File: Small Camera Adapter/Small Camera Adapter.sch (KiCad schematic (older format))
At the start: 6 parts, among them J1 68611514122, J2 10137062-00021LF

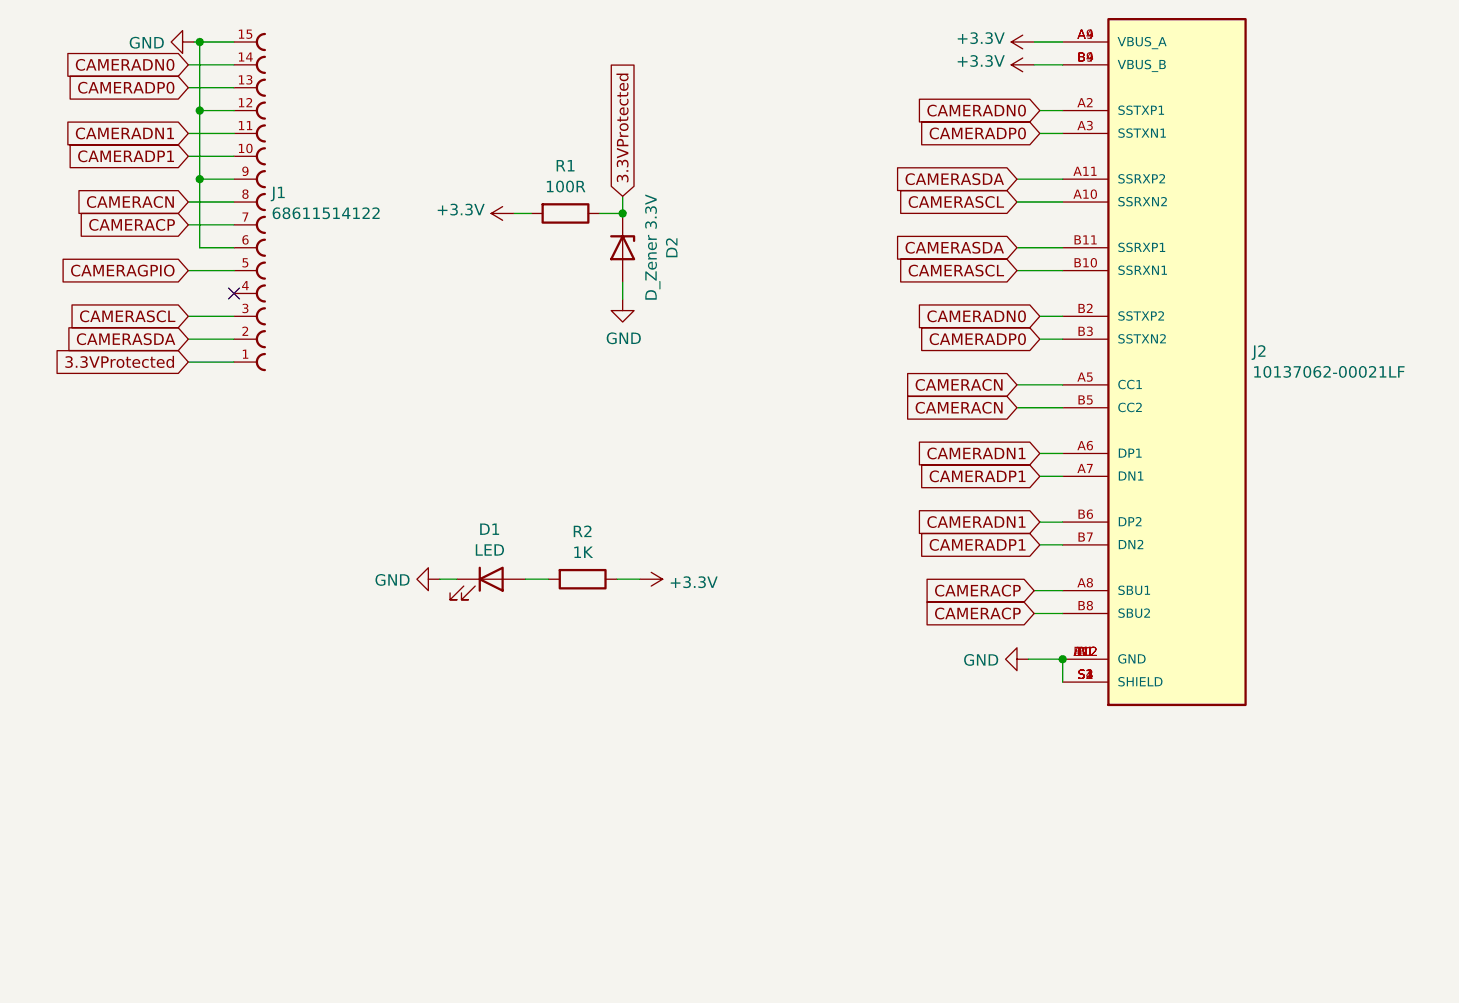
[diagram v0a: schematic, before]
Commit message: Update to camera adapter
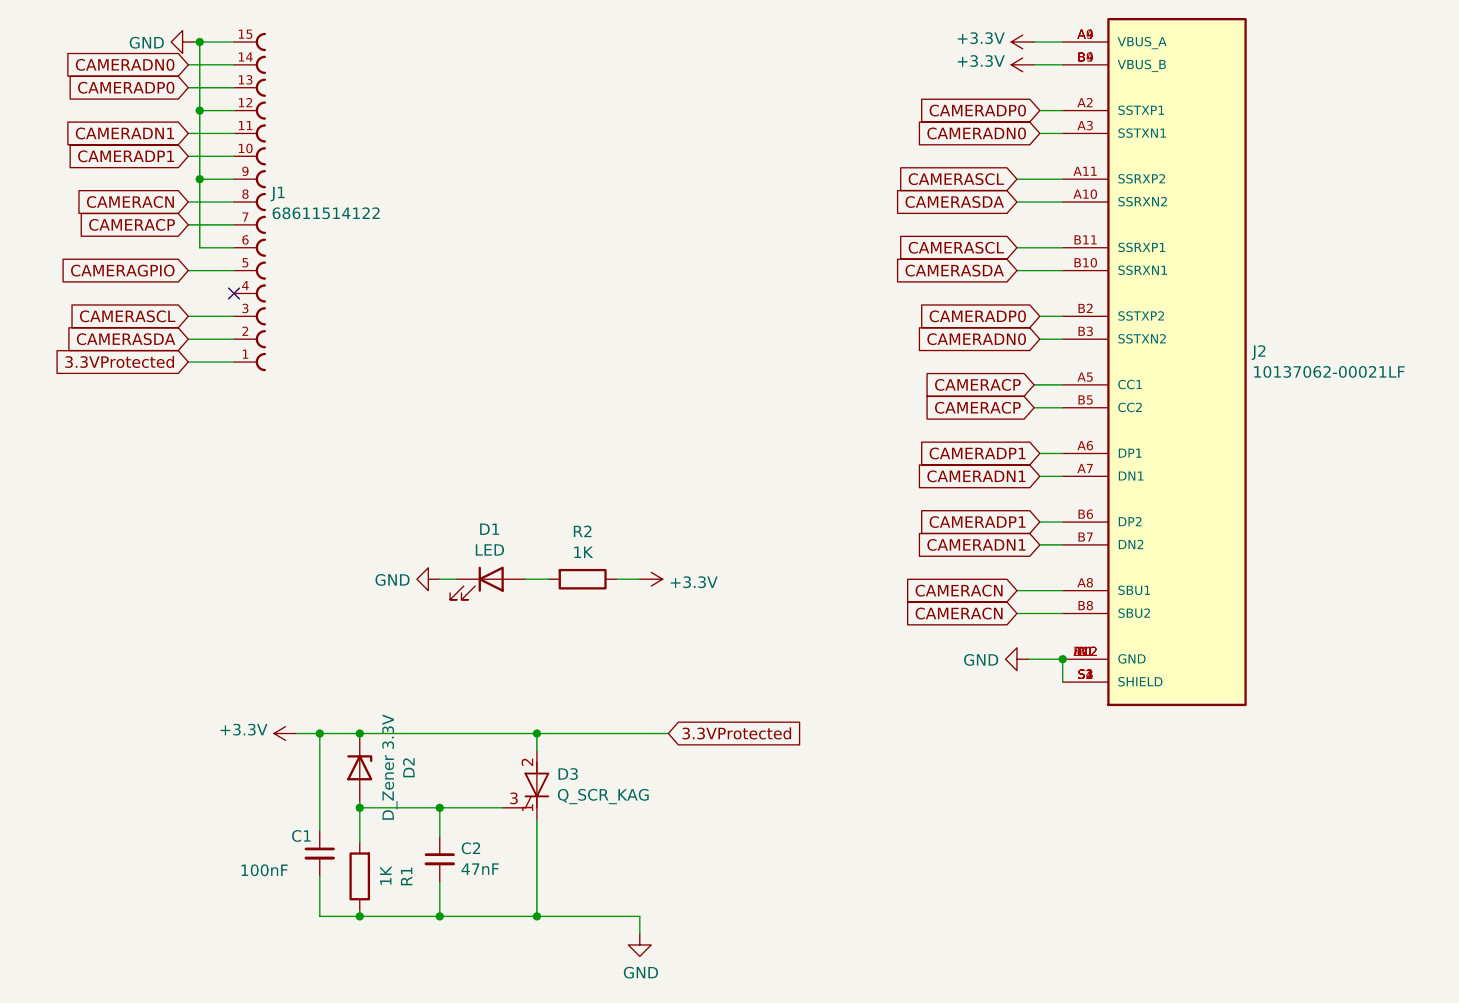
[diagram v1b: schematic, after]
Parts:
- added C1: 100nF, Capacitor_SMD:C_0805_2012Metric_Pad1.18x1.45mm_HandSolder, symbol Device:C_Small
- added C2: 47nF, Capacitor_SMD:C_0805_2012Metric_Pad1.18x1.45mm_HandSolder, symbol Device:C_Small
- added D3: Q_SCR_KAG, digikey-footprints:DPAK, symbol Device:Q_SCR_KAG
- R1: value 100R -> 1K; footprint Resistor_SMD:R_2512_6332Metric_Pad1.40x3.35mm_HandSolder -> Resistor_SMD:R_0805_2012Metric_Pad1.20x1.40mm_HandSolder
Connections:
- net +3V3: now also D2.1 (K), J1.1 (15), C1.1, D3.2 (A); no longer R1.2
- net CAMERACN: now also J2.A8 (SBU1), J2.B8 (SBU2); no longer J2.A5 (CC1), J2.B5 (CC2)
- net CAMERACP: now also J2.A5 (CC1), J2.B5 (CC2); no longer J2.A8 (SBU1), J2.B8 (SBU2)
- net CAMERADN0: now also J2.A3 (SSTXN1), J2.B3 (SSTXN2); no longer J2.A2 (SSTXP1), J2.B2 (SSTXP2)
- net CAMERADN1: now also J2.A7 (DN1), J2.B7 (DN2); no longer J2.A6 (DP1), J2.B6 (DP2)
- net CAMERADP0: now also J2.A2 (SSTXP1), J2.B2 (SSTXP2); no longer J2.A3 (SSTXN1), J2.B3 (SSTXN2)
- net CAMERADP1: now also J2.A6 (DP1), J2.B6 (DP2); no longer J2.A7 (DN1), J2.B7 (DN2)
- net CAMERASCL: now also J2.A11 (SSRXP2), J2.B11 (SSRXP1); no longer J2.A10 (SSRXN2), J2.B10 (SSRXN1)
- net CAMERASDA: now also J2.A10 (SSRXN2), J2.B10 (SSRXN1); no longer J2.A11 (SSRXP2), J2.B11 (SSRXP1)
- net GND: now also R1.1, C1.2, C2.2, D3.1 (K); no longer D2.2 (A)
- removed net 3.3VProtected: D2.1 (K), J1.1 (15), R1.1
- new net: C2.1, D2.2 (A), D3.3 (G), R1.2
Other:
- moved on the sheet: D2, R1
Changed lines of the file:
@@
-$EndComp
-$Comp
-L Device:D_Zener D2
-U 1 1 6026D633
-P 3575 2050
-F 0 "D2" H 3575 2267 50  0000 C CNN
-F 1 "D_Zener 3.3V" H 3575 2176 50  0000 C CNN
-F 2 "Diode_SMD:D_SOD-123F" H 3575 2050 50  0001 C CNN
-F 3 "https://uk.rs-online.com/web/p/zener-diodes/8160608/" H 3575 2050 50  0001 C CNN
-	1    3575 2050
-	0    1    1    0
 $EndComp
 $Comp
@@
 L Device:R R1
 U 1 1 602704B6
-P 3325 1900
-F 0 "R1" V 3118 1900 50  0000 C CNN
-F 1 "100R" V 3209 1900 50  0000 C CNN
-F 2 "Resistor_SMD:R_2512_6332Metric_Pad1.40x3.35mm_HandSolder" V 3255 1900 50  0001 C CNN
-F 3 "https://uk.rs-online.com/web/p/surface-mount-fixed-resistors/7397957/" H 3325 1900 50  0001 C CNN
-	1    3325 1900
-	0    1    1    0
+P 2425 4800
+F 0 "R1" V 2218 4800 50  0000 C CNN
+F 1 "1K" V 2309 4800 50  0000 C CNN
+F 2 "Resistor_SMD:R_0805_2012Metric_Pad1.20x1.40mm_HandSolder" V 2355 4800 50  0001 C CNN
+F 3 "https://uk.rs-online.com/web/p/surface-mount-fixed-resistors/7397957/" H 2425 4800 50  0001 C CNN
+	1    2425 4800
+	-1   0    0    1
 $EndComp
 $Comp
@@
 L power:GND #PWR0105
 U 1 1 6027B84D
-P 3575 2275
-F 0 "#PWR0105" H 3575 2025 50  0001 C CNN
-F 1 "GND" H 3580 2102 50  0000 C CNN
-F 2 "" H 3575 2275 50  0001 C CNN
-F 3 "" H 3575 2275 50  0001 C CNN
-	1    3575 2275
+P 3650 5050
+F 0 "#PWR0105" H 3650 4800 50  0001 C CNN
+F 1 "GND" H 3655 4877 50  0000 C CNN
+F 2 "" H 3650 5050 50  0001 C CNN
+F 3 "" H 3650 5050 50  0001 C CNN
+	1    3650 5050
 	1    0    0    -1
 $EndComp
@@
 L power:+3.3V #PWR0106
 U 1 1 6027C000
-P 3100 1900
-F 0 "#PWR0106" H 3100 1750 50  0001 C CNN
-F 1 "+3.3V" V 3115 2028 50  0000 L CNN
-F 2 "" H 3100 1900 50  0001 C CNN
-F 3 "" H 3100 1900 50  0001 C CNN
-	1    3100 1900
+P 2150 4175
+F 0 "#PWR0106" H 2150 4025 50  0001 C CNN
+F 1 "+3.3V" V 2165 4303 50  0000 L CNN
+F 2 "" H 2150 4175 50  0001 C CNN
+F 3 "" H 2150 4175 50  0001 C CNN
+	1    2150 4175
 	0    -1   -1   0
 $EndComp
 Wire Wire Line
-	3100 1900 3175 1900
-Wire Wire Line
-	3475 1900 3575 1900
-Wire Wire Line
-	3575 2200 3575 2275
+	2150 4175 2250 4175
+Wire Wire Line
+	3650 4975 3650 5050
 Text GLabel 1675 2550 0    50   Input ~ 0
 3.3VProtected
-Text GLabel 3575 1825 1    50   Input ~ 0
+Text GLabel 3775 4175 2    50   Input ~ 0
 3.3VProtected
-Wire Wire Line
-	3575 1825 3575 1900
-Connection ~ 3575 1900
+Text GLabel 5400 1550 0    50   Input ~ 0
+CAMERADN0
 Text GLabel 5400 1450 0    50   Input ~ 0
+CAMERADP0
+Text GLabel 5400 3050 0    50   Input ~ 0
+CAMERADN1
+Text GLabel 5400 2950 0    50   Input ~ 0
+CAMERADP1
+Wire Wire Line
+	5500 1550 5400 1550
+Wire Wire Line
+	5400 1450 5500 1450
+Wire Wire Line
+	5500 3050 5400 3050
+Wire Wire Line
+	5400 2950 5500 2950
+Text GLabel 5375 2750 0    50   Input ~ 0
+CAMERACP
+Text GLabel 5300 2050 0    50   Input ~ 0
+CAMERASCL
+Text GLabel 5300 2150 0    50   Input ~ 0
+CAMERASDA
+Wire Wire Line
+	5500 2050 5300 2050
+Wire Wire Line
+	5300 2150 5500 2150
+Text GLabel 5400 3350 0    50   Input ~ 0
+CAMERADN1
+Text GLabel 5400 3250 0    50   Input ~ 0
+CAMERADP1
+Wire Wire Line
+	5500 3350 5400 3350
+Wire Wire Line
+	5400 3250 5500 3250
+Text GLabel 5400 2450 0    50   Input ~ 0
 CAMERADN0
-Text GLabel 5400 1550 0    50   Input ~ 0
+Text GLabel 5400 2350 0    50   Input ~ 0
 CAMERADP0
-Text GLabel 5400 2950 0    50   Input ~ 0
-CAMERADN1
-Text GLabel 5400 3050 0    50   Input ~ 0
-CAMERADP1
-Wire Wire Line
-	5500 1450 5400 1450
-Wire Wire Line
-	5400 1550 5500 1550
-Wire Wire Line
-	5500 2950 5400 2950
-Wire Wire Line
-	5400 3050 5500 3050
-Text GLabel 5375 3650 0    50   Input ~ 0
+Wire Wire Line
+	5500 2450 5400 2450
+Wire Wire Line
+	5400 2350 5500 2350
+Text GLabel 5375 2650 0    50   Input ~ 0
 CAMERACP
-Text GLabel 5300 2150 0    50   Input ~ 0
-CAMERASCL
-Text GLabel 5300 2050 0    50   Input ~ 0
-CAMERASDA
-Wire Wire Line
-	5500 2150 5300 2150
-Wire Wire Line
-	5300 2050 5500 2050
-Text GLabel 5400 3250 0    50   Input ~ 0
-CAMERADN1
-Text GLabel 5400 3350 0    50   Input ~ 0
-CAMERADP1
-Wire Wire Line
-	5500 3250 5400 3250
-Wire Wire Line
-	5400 3350 5500 3350
-Text GLabel 5400 2350 0    50   Input ~ 0
-CAMERADN0
-Text GLabel 5400 2450 0    50   Input ~ 0
-CAMERADP0
-Wire Wire Line
-	5500 2350 5400 2350
-Wire Wire Line
-	5400 2450 5500 2450
-Text GLabel 5375 3550 0    50   Input ~ 0
-CAMERACP
-Text GLabel 5300 2750 0    50   Input ~ 0
+Text GLabel 5300 3650 0    50   Input ~ 0
 CAMERACN
 Wire Wire Line
-	5300 2750 5500 2750
-Wire Wire Line
-	5500 3650 5375 3650
-Wire Wire Line
-	5375 3550 5500 3550
+	5300 3650 5500 3650
+Wire Wire Line
+	5500 2750 5375 2750
+Wire Wire Line
+	5375 2650 5500 2650
 $Comp
 L power:+3.3V #PWR0107
@@
 Wire Wire Line
 	5500 3850 5350 3850
-Text GLabel 5300 1750 0    50   Input ~ 0
+Text GLabel 5300 1850 0    50   Input ~ 0
 CAMERASDA
 Wire Wire Line
-	5300 1750 5500 1750
+	5300 1850 5500 1850
 $Comp
 L power:+3.3V #PWR0113
@@
 	5500 1150 5375 1150
 Wire Wire Line
-	5500 1850 5300 1850
-Text GLabel 5300 1850 0    50   Input ~ 0
+	5500 1750 5300 1750
+Text GLabel 5300 1750 0    50   Input ~ 0
 CAMERASCL
 Wire Wire Line
-	5500 2650 5300 2650
-Text GLabel 5300 2650 0    50   Input ~ 0
+	5500 3550 5300 3550
+Text GLabel 5300 3550 0    50   Input ~ 0
 CAMERACN
 $Comp
@@
 	5500 3850 5500 3950
 Connection ~ 5500 3850
+$Comp
+L Device:Q_SCR_KAG D3
+U 1 1 60304FE2
+P 3200 4400
+F 0 "D3" H 3288 4446 50  0000 L CNN
+F 1 "Q_SCR_KAG" H 3288 4355 50  0000 L CNN
+F 2 "digikey-footprints:DPAK" V 3200 4400 50  0001 C CNN
+F 3 "~" V 3200 4400 50  0001 C CNN
+	1    3200 4400
+	1    0    0    -1
+$EndComp
+Wire Wire Line
+	3050 4500 2775 4500
+Wire Wire Line
+	2425 4500 2425 4475
+Wire Wire Line
+	2425 4500 2425 4650
+Connection ~ 2425 4500
+Wire Wire Line
+	2425 4175 3200 4175
+Connection ~ 2425 4175
+Wire Wire Line
+	3200 4250 3200 4175
+Wire Wire Line
+	3200 4175 3775 4175
+Wire Wire Line
+	3200 4550 3200 4975
+Wire Wire Line
+	3200 4975 3650 4975
+Wire Wire Line
+	2425 4950 2425 4975
+Wire Wire Line
+	2425 4975 2775 4975
+Connection ~ 3200 4175
+Connection ~ 3200 4975
+$Comp
+L Device:C_Small C2
+U 1 1 6031A6F9
+P 2775 4725
+F 0 "C2" H 2867 4771 50  0000 L CNN
+F 1 "47nF" H 2867 4680 50  0000 L CNN
+F 2 "Capacitor_SMD:C_0805_2012Metric_Pad1.18x1.45mm_HandSolder" H 2775 4725 50  0001 C CNN
+F 3 "~" H 2775 4725 50  0001 C CNN
+	1    2775 4725
+	1    0    0    -1
+$EndComp
+$Comp
+L Device:C_Small C1
+U 1 1 6031ADFF
+P 2250 4700
+F 0 "C1" H 2125 4775 50  0000 L CNN
+F 1 "100nF" H 1900 4625 50  0000 L CNN
+F 2 "Capacitor_SMD:C_0805_2012Metric_Pad1.18x1.45mm_HandSolder" H 2250 4700 50  0001 C CNN
+F 3 "~" H 2250 4700 50  0001 C CNN
+	1    2250 4700
+	1    0    0    -1
+$EndComp
+Wire Wire Line
+	2250 4600 2250 4175
+Connection ~ 2250 4175
+Wire Wire Line
+	2250 4175 2425 4175
+Wire Wire Line
+	2250 4800 2250 4975
+Wire Wire Line
+	2250 4975 2425 4975
+Connection ~ 2425 4975
+Wire Wire Line
+	2775 4625 2775 4500
+Connection ~ 2775 4500
+Wire Wire Line
+	2775 4500 2425 4500
+Wire Wire Line
+	2775 4825 2775 4975
+Connection ~ 2775 4975
+Wire Wire Line
+	2775 4975 3200 4975
+$Comp
+L Device:D_Zener D2
+U 1 1 6026D633
+P 2425 4325
+F 0 "D2" H 2425 4542 50  0000 C CNN
+F 1 "D_Zener 3.3V" H 2425 4451 50  0000 C CNN
+F 2 "Diode_SMD:D_SOD-123F" H 2425 4325 50  0001 C CNN
+F 3 "https://uk.rs-online.com/web/p/zener-diodes/8160608/" H 2425 4325 50  0001 C CNN
+	1    2425 4325
+	0    1    1    0
+$EndComp
 $EndSCHEMATC
